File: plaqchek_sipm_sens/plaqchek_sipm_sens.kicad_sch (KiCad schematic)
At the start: 54 parts, among them J1 Conn_01x04, J3 Conn_01x05, U11 LDK320AM-R, U14 MIC5504-1.8YM5, U5 TPS7A2050PDBVR, U8 MC79M05_TO252, U8 RT9072BGB

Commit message: add sipm footprints, sensing board layout
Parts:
- J1: footprint Resistor_SMD:R_0603_1608Metric_Pad0.98x0.95mm_HandSolder -> Connector_PinHeader_2.54mm:PinHeader_1x04_P2.54mm_Vertical
- J3: footprint Resistor_SMD:R_0603_1608Metric_Pad0.98x0.95mm_HandSolder -> Connector_PinHeader_2.54mm:PinHeader_1x05_P2.54mm_Vertical
- TP1, TP10, TP13, TP14, TP2, TP3, TP4, TP6, TP8, TP9: footprint TestPoint:TestPoint_Pad_1.5x1.5mm -> TestPoint:TestPoint_Pad_D1.0mm
- U8: footprint Package_TO_SOT_SMD:TO-252-3_TabPin2 -> Package_TO_SOT_SMD:TO-252-2
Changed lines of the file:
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@@
       (effects (font (size 1.27 1.27)) (justify left))
     )
-    (property "Footprint" "TestPoint:TestPoint_Pad_1.5x1.5mm" (at 99.06 135.255 0)
+    (property "Footprint" "TestPoint:TestPoint_Pad_D1.0mm" (at 99.06 135.255 0)
       (effects (font (size 1.27 1.27)) hide)
     )
@@
       (effects (font (size 1.27 1.27)) (justify left))
     )
-    (property "Footprint" "TestPoint:TestPoint_Pad_1.5x1.5mm" (at 159.385 88.9 0)
+    (property "Footprint" "TestPoint:TestPoint_Pad_D1.0mm" (at 159.385 88.9 0)
       (effects (font (size 1.27 1.27)) hide)
     )
@@
       (effects (font (size 1.27 1.27)) (justify left))
     )
-    (property "Footprint" "TestPoint:TestPoint_Pad_1.5x1.5mm" (at 122.555 170.18 0)
+    (property "Footprint" "TestPoint:TestPoint_Pad_D1.0mm" (at 122.555 170.18 0)
       (effects (font (size 1.27 1.27)) hide)
     )
@@
       (effects (font (size 1.27 1.27)) (justify left))
     )
-    (property "Footprint" "TestPoint:TestPoint_Pad_1.5x1.5mm" (at 247.015 90.17 0)
+    (property "Footprint" "TestPoint:TestPoint_Pad_D1.0mm" (at 247.015 90.17 0)
       (effects (font (size 1.27 1.27)) hide)
     )
@@
       (effects (font (size 1.27 1.27)))
     )
-    (property "Footprint" "Resistor_SMD:R_0603_1608Metric_Pad0.98x0.95mm_HandSolder" (at 79.375 31.75 0)
+    (property "Footprint" "Connector_PinHeader_2.54mm:PinHeader_1x04_P2.54mm_Vertical" (at 79.375 31.75 0)
       (effects (font (size 1.27 1.27)) hide)
     )
@@
       (effects (font (size 1.27 1.27)))
     )
-    (property "Footprint" "Resistor_SMD:R_0603_1608Metric_Pad0.98x0.95mm_HandSolder" (at 26.035 34.29 0)
+    (property "Footprint" "Connector_PinHeader_2.54mm:PinHeader_1x05_P2.54mm_Vertical" (at 26.035 34.29 0)
       (effects (font (size 1.27 1.27)) hide)
     )
@@
       (effects (font (size 1.27 1.27)))
     )
-    (property "Footprint" "Package_TO_SOT_SMD:TO-252-3_TabPin2" (at 211.455 153.67 0)
+    (property "Footprint" "Package_TO_SOT_SMD:TO-252-2" (at 211.455 153.67 0)
       (effects (font (size 1.27 1.27) italic) hide)
     )
@@
       (effects (font (size 1.27 1.27)) (justify left))
     )
-    (property "Footprint" "TestPoint:TestPoint_Pad_1.5x1.5mm" (at 188.595 147.32 0)
+    (property "Footprint" "TestPoint:TestPoint_Pad_D1.0mm" (at 188.595 147.32 0)
       (effects (font (size 1.27 1.27)) hide)
     )
@@
       (effects (font (size 1.27 1.27)) (justify left))
     )
-    (property "Footprint" "TestPoint:TestPoint_Pad_1.5x1.5mm" (at 238.125 146.05 0)
+    (property "Footprint" "TestPoint:TestPoint_Pad_D1.0mm" (at 238.125 146.05 0)
       (effects (font (size 1.27 1.27)) hide)
     )
@@
       (effects (font (size 1.27 1.27)) (justify left))
     )
-    (property "Footprint" "TestPoint:TestPoint_Pad_1.5x1.5mm" (at 135.255 170.18 0)
+    (property "Footprint" "TestPoint:TestPoint_Pad_D1.0mm" (at 135.255 170.18 0)
       (effects (font (size 1.27 1.27)) hide)
     )
@@
       (effects (font (size 1.27 1.27)) (justify left))
     )
-    (property "Footprint" "TestPoint:TestPoint_Pad_1.5x1.5mm" (at 121.92 135.255 0)
+    (property "Footprint" "TestPoint:TestPoint_Pad_D1.0mm" (at 121.92 135.255 0)
       (effects (font (size 1.27 1.27)) hide)
     )
@@
       (effects (font (size 1.27 1.27)) (justify left))
     )
-    (property "Footprint" "TestPoint:TestPoint_Pad_1.5x1.5mm" (at 55.88 90.17 0)
+    (property "Footprint" "TestPoint:TestPoint_Pad_D1.0mm" (at 55.88 90.17 0)
       (effects (font (size 1.27 1.27)) hide)
     )
@@
       (effects (font (size 1.27 1.27)) (justify left))
     )
-    (property "Footprint" "TestPoint:TestPoint_Pad_1.5x1.5mm" (at 54.61 171.45 0)
+    (property "Footprint" "TestPoint:TestPoint_Pad_D1.0mm" (at 54.61 171.45 0)
       (effects (font (size 1.27 1.27)) hide)
     )
@@
       (effects (font (size 1.27 1.27)) (justify left))
     )
-    (property "Footprint" "TestPoint:TestPoint_Pad_1.5x1.5mm" (at 256.54 146.05 0)
+    (property "Footprint" "TestPoint:TestPoint_Pad_D1.0mm" (at 256.54 146.05 0)
       (effects (font (size 1.27 1.27)) hide)
     )
@@
       (effects (font (size 1.27 1.27)) (justify left))
     )
-    (property "Footprint" "TestPoint:TestPoint_Pad_1.5x1.5mm" (at 53.34 136.525 0)
+    (property "Footprint" "TestPoint:TestPoint_Pad_D1.0mm" (at 53.34 136.525 0)
       (effects (font (size 1.27 1.27)) hide)
     )
@@
       (effects (font (size 1.27 1.27)) (justify left))
     )
-    (property "Footprint" "TestPoint:TestPoint_Pad_1.5x1.5mm" (at 146.685 88.9 0)
-      (effects (font (size 1.27 1.27)) hide)
-    )
+    (property "Footprint" "TestPoint:TestPoint_Pad_D1.0mm" (at 146.685 88.9 0)
+      (effects (font (size 1.27 1.27)) hide)
+    )

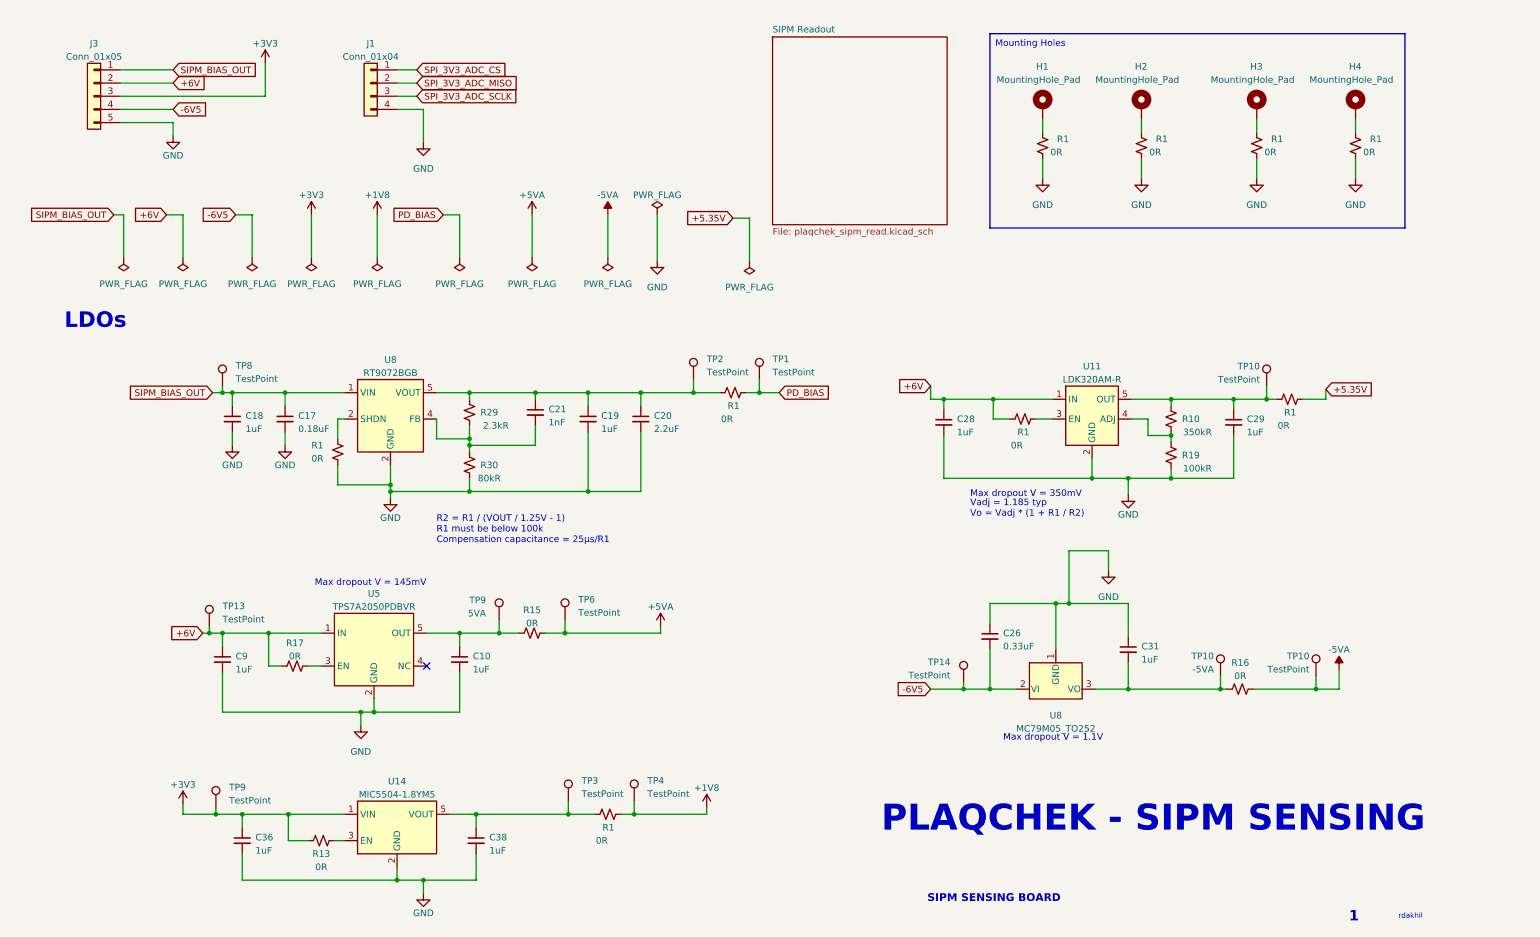
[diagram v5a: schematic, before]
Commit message: start sensor board routing
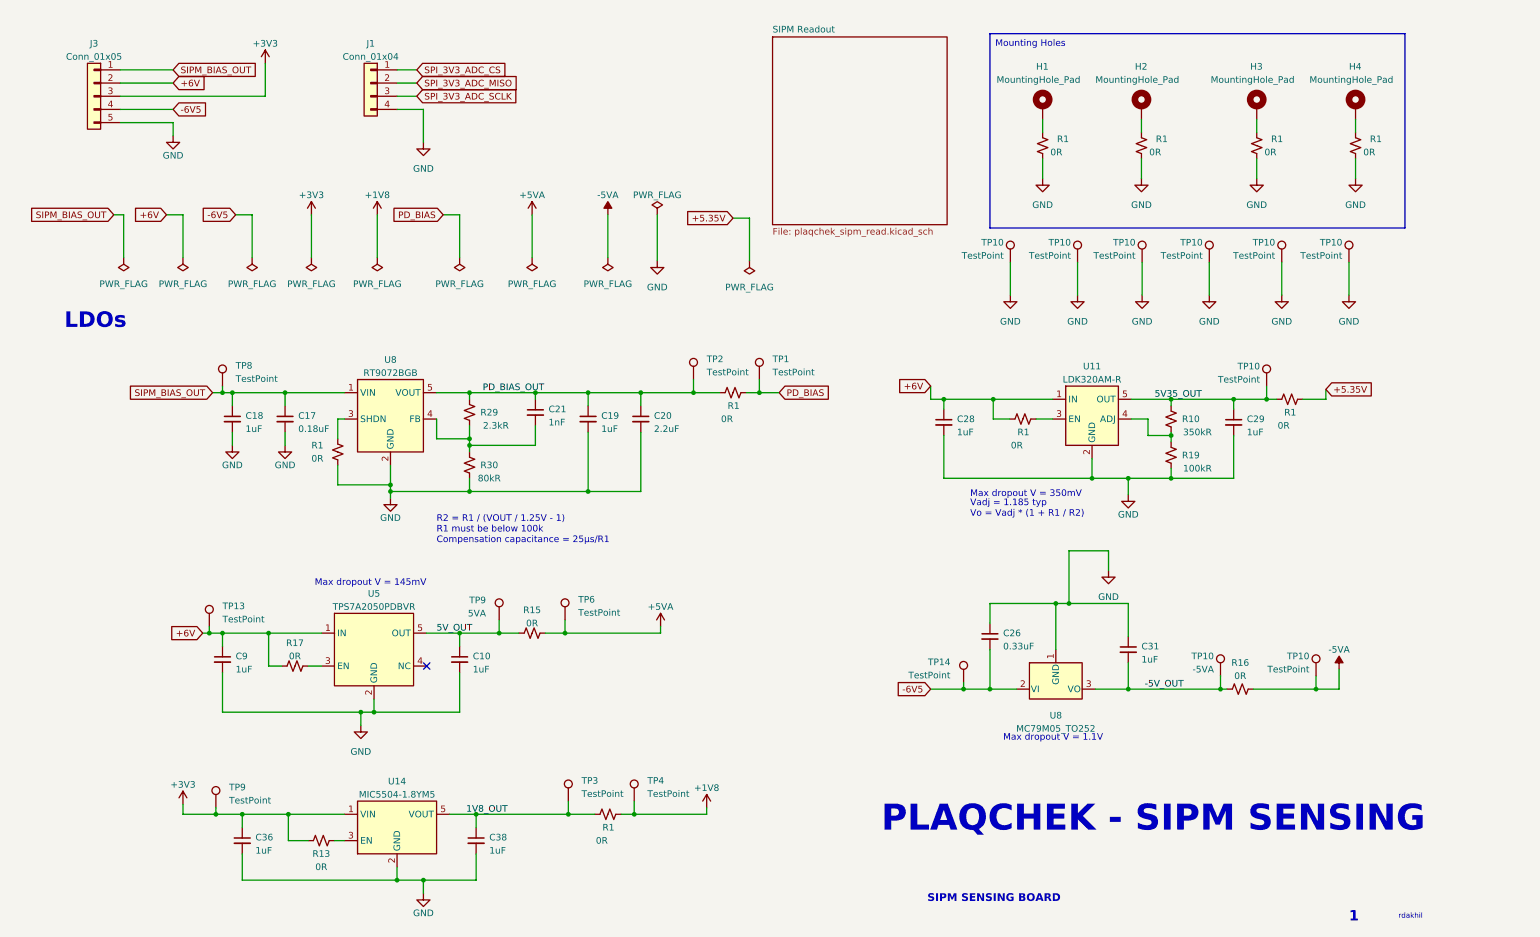
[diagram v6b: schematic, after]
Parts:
- added TP10 (x6): TestPoint, TestPoint:TestPoint_Pad_D1.0mm, symbol Connector:TestPoint
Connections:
- net GND: now also TP10.1, TP10.1, TP10.1, TP10.1, TP10.1, TP10.1
- net 5V_OUT: now reaches C10.1, R15.2, TP9.1, U5.5 (OUT)
- net PD_BIAS_OUT: now reaches C19.1, C20.1, C21.1, R1.2, R29.1, TP2.1, U8.5 (VOUT)
- net 1V8_OUT: now reaches C38.1, R1.2, TP3.1, U14.5 (VOUT)
- net 5V35_OUT: now reaches C29.1, R1.2, R10.1, TP10.1, U11.5 (OUT)
- net -5V_OUT: now reaches C31.2, R16.2, TP10.1, U8.3 (VO)
- net at R1.2: now also U8.3 (SHDN); no longer U8.2 (SHDN)

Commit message: finish routing sipm board
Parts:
- H1, H2, H3, H4: footprint MountingHole:MountingHole_3.2mm_M3_Pad_Via -> MountingHole:MountingHole_3.2mm_M3_Pad
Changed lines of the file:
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@@
       (effects (font (size 1.27 1.27)) (justify left))
     )
-    (property "Footprint" "MountingHole:MountingHole_3.2mm_M3_Pad_Via" (at 269.24 36.195 0)
+    (property "Footprint" "MountingHole:MountingHole_3.2mm_M3_Pad" (at 269.24 36.195 0)
       (effects (font (size 1.27 1.27)) hide)
     )
@@
       (effects (font (size 1.27 1.27)) (justify left))
     )
-    (property "Footprint" "MountingHole:MountingHole_3.2mm_M3_Pad_Via" (at 227.965 36.195 0)
+    (property "Footprint" "MountingHole:MountingHole_3.2mm_M3_Pad" (at 227.965 36.195 0)
       (effects (font (size 1.27 1.27)) hide)
     )
@@
       (effects (font (size 1.27 1.27)) (justify left))
     )
-    (property "Footprint" "MountingHole:MountingHole_3.2mm_M3_Pad_Via" (at 208.915 36.195 0)
+    (property "Footprint" "MountingHole:MountingHole_3.2mm_M3_Pad" (at 208.915 36.195 0)
       (effects (font (size 1.27 1.27)) hide)
     )
@@
       (effects (font (size 1.27 1.27)) (justify left))
     )
-    (property "Footprint" "MountingHole:MountingHole_3.2mm_M3_Pad_Via" (at 250.19 36.195 0)
-      (effects (font (size 1.27 1.27)) hide)
-    )
+    (property "Footprint" "MountingHole:MountingHole_3.2mm_M3_Pad" (at 250.19 36.195 0)
+      (effects (font (size 1.27 1.27)) hide)
+    )
